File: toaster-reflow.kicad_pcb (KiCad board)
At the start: 2 copper layers, 41.9 x 63.5 mm, 40 parts, among them J1 1935161, J2 1935161, J3 Raspberry_Pi_2_3, J4 1935161, J5 1935161, J6 Conn_01x03, K1 1-1415899-3, Q1 Q_PMOS_GSD, Q2 Q_PMOS_GSD, Q3 Q_PMOS_GSD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

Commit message: update pcb
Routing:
- net Net-(J1-Pad2): track 16.7 -> 0.00 mm
- net Net-(J1-Pad1): track 16.7 -> 0.00 mm
- added copper zone on B.Cu, net Net-(J1-Pad1)
- added copper zone on F.Cu, net Net-(J1-Pad1)
- added copper zone on B.Cu, net Net-(J1-Pad2)
- added copper zone on F.Cu, net Net-(J1-Pad2)
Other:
- outline, holes or cut-outs redrawn
- net class AC_Load: clearance 0.2 -> 1
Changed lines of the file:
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@@
   (general
     (thickness 1.6)
-    (drawings 20)
-    (tracks 363)
+    (drawings 8)
+    (tracks 357)
     (zones 0)
     (modules 40)
@@
     (last_trace_width 0.25)
     (trace_clearance 0.2)
-    (zone_clearance 0.508)
+    (zone_clearance 2)
     (zone_45_only no)
     (trace_min 0.2)
@@
   )
   (net_class AC_Load ""
-    (clearance 0.2)
+    (clearance 1)
     (trace_width 3)
     (via_dia 0.8)
@@
     (add_net "Net-(C7-Pad2)")
     (add_net "Net-(C8-Pad2)")
+  )
+  (module 1935161:PHOENIX_1935161 (layer F.Cu)
+    (at 132.08 93.98 90)
+    (fp_text reference J1 (at 0 0 90) (layer F.SilkS)
+      (effects (font (size 1 0.9) (thickness 0.05)))
+    )
+    (fp_text value 1935161 (at 0 0 90) (layer F.SilkS)
+      (effects (font (size 1 0.9) (thickness 0.05)))
+    )
+    (fp_line (start -5 -4) (end 5 -4) (layer F.SilkS) (width 0.127))
+    (fp_line (start 5 -4) (end 5 4.3) (layer F.SilkS) (width 0.127))
+    (fp_line (start 5 4.3) (end -5 4.3) (layer F.SilkS) (width 0.127))
+    (fp_line (start -5 4.3) (end -5 -4) (layer F.SilkS) (width 0.127))
+    (fp_line (start -5 4.3) (end -5 -4) (layer Dwgs.User) (width 0.127))
+    (fp_line (start -5 -4) (end 5 -4) (layer Dwgs.User) (width 0.127))
+    (fp_line (start 5 -4) (end 5 4.3) (layer Dwgs.User) (width 0.127))
+    (fp_line (start 5 4.3) (end -5 4.3) (layer Dwgs.User) (width 0.127))
+    (fp_circle (center -3.8 -1.5) (end -3.66 -1.5) (layer F.SilkS) (width 0.28))
+    (fp_circle (center -3.8 -1.5) (end -3.66 -1.5) (layer Dwgs.User) (width 0.28))
+    (fp_line (start -5.25 -4.25) (end 5.25 -4.25) (layer Eco1.User) (width 0.05))
+    (fp_line (start 5.25 -4.25) (end 5.25 4.55) (layer Eco1.User) (width 0.05))
+    (fp_line (start 5.25 4.55) (end -5.25 4.55) (layer Eco1.User) (width 0.05))
+    (fp_line (start -5.25 4.55) (end -5.25 -4.25) (layer Eco1.User) (width 0.05))
+    (fp_text user NAME (at -5.090826 -5.090826 90) (layer Cmts.User)
+      (effects (font (size 1 1) (thickness 0.05)))
+    )
+    (fp_text user VALUE (at -5.093458 6.366825 90) (layer Eco2.User)
+      (effects (font (size 1 1) (thickness 0.05)))
+    )
+    (pad 1 thru_hole rect (at -2.5 0 90) (size 1.95 1.95) (drill 1.3) (layers *.Cu *.Mask)
+      (net 16 "Net-(J1-Pad1)"))
+    (pad 2 thru_hole circle (at 2.5 0 90) (size 1.95 1.95) (drill 1.3) (layers *.Cu *.Mask)
+      (net 17 "Net-(J1-Pad2)"))
   )
   (module Capacitor_SMD:C_0603_1608Metric (layer F.Cu)
@@
       (rotate (xyz 0 0 0))
     )
-  )
-  (module 1935161:PHOENIX_1935161 (layer F.Cu)
-    (at 132.08 93.98 90)
-    (fp_text reference J1 (at 0 0 90) (layer F.SilkS)
-      (effects (font (size 1 0.9) (thickness 0.05)))
-    )
-    (fp_text value 1935161 (at 0 0 90) (layer F.SilkS)
-      (effects (font (size 1 0.9) (thickness 0.05)))
-    )
-    (fp_line (start -5 -4) (end 5 -4) (layer F.SilkS) (width 0.127))
-    (fp_line (start 5 -4) (end 5 4.3) (layer F.SilkS) (width 0.127))
-    (fp_line (start 5 4.3) (end -5 4.3) (layer F.SilkS) (width 0.127))
-    (fp_line (start -5 4.3) (end -5 -4) (layer F.SilkS) (width 0.127))
-    (fp_line (start -5 4.3) (end -5 -4) (layer Dwgs.User) (width 0.127))
-    (fp_line (start -5 -4) (end 5 -4) (layer Dwgs.User) (width 0.127))
-    (fp_line (start 5 -4) (end 5 4.3) (layer Dwgs.User) (width 0.127))
-    (fp_line (start 5 4.3) (end -5 4.3) (layer Dwgs.User) (width 0.127))
-    (fp_circle (center -3.8 -1.5) (end -3.66 -1.5) (layer F.SilkS) (width 0.28))
-    (fp_circle (center -3.8 -1.5) (end -3.66 -1.5) (layer Dwgs.User) (width 0.28))
-    (fp_line (start -5.25 -4.25) (end 5.25 -4.25) (layer Eco1.User) (width 0.05))
-    (fp_line (start 5.25 -4.25) (end 5.25 4.55) (layer Eco1.User) (width 0.05))
-    (fp_line (start 5.25 4.55) (end -5.25 4.55) (layer Eco1.User) (width 0.05))
-    (fp_line (start -5.25 4.55) (end -5.25 -4.25) (layer Eco1.User) (width 0.05))
-    (fp_text user NAME (at -5.090826 -5.090826 90) (layer Cmts.User)
-      (effects (font (size 1 1) (thickness 0.05)))
-    )
-    (fp_text user VALUE (at -5.093458 6.366825 90) (layer Eco2.User)
-      (effects (font (size 1 1) (thickness 0.05)))
-    )
-    (pad 1 thru_hole rect (at -2.5 0 90) (size 1.95 1.95) (drill 1.3) (layers *.Cu *.Mask)
-      (net 16 "Net-(J1-Pad1)"))
-    (pad 2 thru_hole circle (at 2.5 0 90) (size 1.95 1.95) (drill 1.3) (layers *.Cu *.Mask)
-      (net 17 "Net-(J1-Pad2)"))
   )
   (module 1935161:PHOENIX_1935161 (layer F.Cu)
@@
     )
   )
-  (gr_arc (start 129.794 93.98) (end 129.794 93.472) (angle -180) (layer Edge.Cuts) (width 0.2))
-  (gr_arc (start 150.876 93.472) (end 150.876 93.98) (angle -180) (layer Edge.Cuts) (width 0.2))
-  (gr_line (start 148.844 92.964) (end 150.876 92.964) (layer Edge.Cuts) (width 0.2))
-  (gr_line (start 148.844 93.98) (end 150.876 93.98) (layer Edge.Cuts) (width 0.2))
-  (gr_line (start 132.08 94.488) (end 129.794 94.488) (layer Edge.Cuts) (width 0.2))
-  (gr_line (start 132.08 93.472) (end 129.794 93.472) (layer Edge.Cuts) (width 0.2))
-  (gr_line (start 132.08 94.488) (end 137.414 94.488) (layer Edge.Cuts) (width 0.2))
-  (gr_line (start 137.414 93.472) (end 132.08 93.472) (layer Edge.Cuts) (width 0.2))
-  (gr_line (start 140.97 92.964) (end 137.414 93.472) (layer Edge.Cuts) (width 0.2))
-  (gr_line (start 148.844 92.964) (end 140.97 92.964) (layer Edge.Cuts) (width 0.2))
-  (gr_line (start 140.97 93.98) (end 148.844 93.98) (layer Edge.Cuts) (width 0.2))
-  (gr_line (start 137.414 94.488) (end 140.97 93.98) (layer Edge.Cuts) (width 0.2))
   (gr_text Heating (at 128.27 123.19) (layer F.SilkS)
     (effects (font (size 1.5 1.5) (thickness 0.3)) (justify left))
@@
   (segment (start 156.9975 137.16) (end 157.48 136.6775) (width 0.25) (layer F.Cu) (net 15))
   (segment (start 153.1875 137.16) (end 156.9975 137.16) (width 0.25) (layer F.Cu) (net 15))
-  (segment (start 148.53 95.99) (end 141.03 95.99) (width 3) (layer B.Cu) (net 16) (status 30))
-  (segment (start 140.54 96.48) (end 132.08 96.48) (width 3) (layer B.Cu) (net 16) (status 30))
-  (segment (start 141.03 95.99) (end 140.54 96.48) (width 3) (layer B.Cu) (net 16) (status 30))
-  (segment (start 132.61 90.95) (end 141.03 90.95) (width 3) (layer B.Cu) (net 17) (status 30))
-  (segment (start 132.08 91.48) (end 132.61 90.95) (width 3) (layer B.Cu) (net 17) (status 30))
-  (segment (start 141.03 90.95) (end 148.53 90.95) (width 3) (layer B.Cu) (net 17) (status 30))
   (segment (start 157.2675 100.6) (end 157.48 100.8125) (width 0.25) (layer F.Cu) (net 24) (status 30))
   (segment (start 154.62 100.6) (end 157.2675 100.6) (width 0.25) (layer F.Cu) (net 24) (status 30))
@@
     )
   )
-  (zone (net 0) (net_name "") (layers F&B.Cu) (hatch edge 0.508)
-    (connect_pads (clearance 0.508))
+  (zone (net 16) (net_name "Net-(J1-Pad1)") (layer F.Cu) (hatch edge 0.508)
+    (priority 1)
+    (connect_pads yes (clearance 2))
     (min_thickness 0.254)
-    (keepout (tracks allowed) (vias allowed) (copperpour not_allowed))
-    (fill (arc_segments 16) (thermal_gap 0.508) (thermal_bridge_width 0.508))
+    (fill yes (arc_segments 16) (thermal_gap 0.25) (thermal_bridge_width 0.508))
     (polygon
       (pts
-        (xy 127.508 88.138) (xy 152.146 88.138) (xy 152.146 99.06) (xy 127.508 99.06)
+        (xy 127 94.742) (xy 127 100.33) (xy 150.114 100.33) (xy 150.114 94.234) (xy 140.97 94.234)
+        (xy 137.668 94.742)
       )
     )
+  )
+  (zone (net 17) (net_name "Net-(J1-Pad2)") (layer F.Cu) (hatch edge 0.508)
+    (priority 1)
+    (connect_pads yes (clearance 2))
+    (min_thickness 0.254)
+    (fill yes (arc_segments 16) (thermal_gap 1) (thermal_bridge_width 0.508))
+    (polygon
+      (pts
+        (xy 150.114 92.71) (xy 140.97 92.71) (xy 137.414 93.218) (xy 127 93.218) (xy 127 87.63)
+        (xy 150.114 87.63)
+      )
+    )
+  )
+  (zone (net 17) (net_name "Net-(J1-Pad2)") (layer B.Cu) (hatch edge 0.508)
+    (priority 2)
+    (connect_pads yes (clearance 2))
+    (min_thickness 0.254)
+    (fill yes (arc_segments 16) (thermal_gap 1) (thermal_bridge_width 0.508))
+    (polygon
+      (pts
+        (xy 127 87.63) (xy 150.114 87.63) (xy 150.114 92.71) (xy 140.97 92.71) (xy 137.668 93.218)
+        (xy 127 93.218)
+      )
+    )
+  )
+  (zone (net 16) (net_name "Net-(J1-Pad1)") (layer B.Cu) (hatch edge 0.508)
+    (priority 2)
+    (connect_pads yes (clearance 2))
+    (min_thickness 0.254)
+    (fill yes (arc_segments 16) (thermal_gap 1) (thermal_bridge_width 0.508))
+    (polygon
+      (pts
+        (xy 127 94.742) (xy 137.922 94.742) (xy 140.97 94.234) (xy 150.114 94.234) (xy 150.114 100.33)
+        (xy 127 100.33)
+      )
+    )

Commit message: Add a bunch of stuff
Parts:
- removed J5: 1935161, 1935161:PHOENIX_1935161
- removed Q5: Q_PMOS_GSD, Package_TO_SOT_SMD:SOT-23
- added R10: 100, Resistor_SMD:R_0603_1608Metric, B.Cu at (125.2, 122.4)
- added R11: 47k, Resistor_SMD:R_0603_1608Metric, B.Cu at (147.8, 123.7)
- added R9: 100, Resistor_SMD:R_0603_1608Metric, B.Cu at (133.3, 118.4)
- C1, C2, C3, C4, C7, C8, C9, D1, R1, R4, R5, U1, U2, U3: moved to B.Cu
- J4: value 1935161 -> Conn_01x04; footprint 1935161:PHOENIX_1935161 -> 1990025:1990025
- Q1, Q2: value Q_PMOS_GSD -> Q_NMOS_GSD; footprint Package_TO_SOT_SMD:SOT-23 -> Package_TO_SOT_SMD:SC-59; moved to B.Cu
- Q3, Q4: value Q_PMOS_GSD -> Q_PNP_BEC; footprint Package_TO_SOT_SMD:SOT-23 -> Package_TO_SOT_SMD:SC-59; moved to B.Cu
- R2: value 470 -> 1K
- R6: value 10K -> 100; moved to B.Cu
- R7: value 470 -> 100; moved to B.Cu
- R8: value 470 -> 47k; moved to B.Cu
- moved R7 44.8 mm to (126.5, 112.0), turned to 270 degrees
- moved D4 36.4 mm to (137.7, 116.8)
- moved C2 36.0 mm to (133.1, 113.0), turned to 180 degrees
- moved C6 35.2 mm to (142.0, 112.8), turned to 180 degrees
- moved J2 34.3 mm to (128.8, 99.8), turned to 270 degrees
- moved C3 34.2 mm to (128.5, 112.0)
- moved C5 33.8 mm to (140.2, 114.8), turned to 180 degrees
- moved D2 32.1 mm to (126.2, 88.9)
- moved R2 31.9 mm to (131.3, 88.9)
- moved R6 31.1 mm to (129.3, 114.8), turned to 0 degrees
- moved C4 30.4 mm to (133.1, 111.0), turned to 0 degrees
- moved U2 29.4 mm to (140.5, 115.6)
- moved J6 28.3 mm to (131.3, 106.9), turned to 270 degrees
- moved J3 26.3 mm to (157.0, 74.9)
- moved C7 24.2 mm to (124.5, 117.3), turned to 0 degrees
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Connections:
- D1 pad 1: Net-(D1-Pad1) -> +5V
- D1 pad 2: GND -> Net-(D1-Pad2)
- D2 pad 2: Net-(D1-Pad1) -> +5V
- D3 pad 1: Net-(D3-Pad1) -> GND
- D3 pad 2: +3V3 -> Net-(D3-Pad2)
- D4 pad 1: Net-(D4-Pad1) -> GND
- D5 pad 1: Net-(D5-Pad1) -> GND
- J2 pad 1: GND -> +5V
- J2 pad 2: +5V -> GND
- J4 pad 1: Net-(C3-Pad2) -> /Thermocouple2/T-
- J4 pad 2: Net-(C2-Pad2) -> /Thermocouple2/T+
- J6 pad 1: Net-(J6-Pad1) -> /SERVO_PWM
- K1 pad 11_1: Net-(J1-Pad1) -> Net-(J1-Pad2)
- K1 pad 11_2: Net-(J1-Pad1) -> Net-(J1-Pad2)
- K1 pad 14_1: Net-(J1-Pad2) -> Net-(J1-Pad1)
- K1 pad 14_2: Net-(J1-Pad2) -> Net-(J1-Pad1)
- K1 pad A1: Net-(D1-Pad1) -> +5V
- K1 pad A2: GND -> Net-(D1-Pad2)
- LS1 pad 2: GND -> Net-(LS1-Pad2)
- Q1 pad 2: Net-(D1-Pad1) -> GND
- Q1 pad 3: +3V3 -> Net-(D1-Pad2)
- Q2 pad 2: Net-(LS1-Pad1) -> GND
- Q2 pad 3: +3V3 -> Net-(LS1-Pad2)
- Q3 pad 1: /SERVO_PWM -> Net-(Q3-Pad1)
- Q3 pad 2: Net-(J6-Pad1) -> Net-(D4-Pad2)
- Q4 pad 1: /THERMO1_FAULT -> Net-(Q4-Pad1)
- Q4 pad 2: Net-(D4-Pad2) -> Net-(D5-Pad2)
- R1 pad 1: +3V3 -> /HEAT_ENABLE
- R1 pad 2: /HEAT_ENABLE -> GND
- R2 pad 1: GND -> Net-(D1-Pad2)
- R3 pad 1: GND -> Net-(D3-Pad2)
- R3 pad 2: Net-(D3-Pad1) -> +3V3
- R4 pad 1: +3V3 -> /BUZZER
- R4 pad 2: /BUZZER -> GND
- R5 pad 2: GND -> Net-(LS1-Pad2)
- R6 pad 1: +3V3 -> Net-(C2-Pad2)
- R6 pad 2: /SERVO_PWM -> /Thermocouple1/T+
- R7 pad 1: GND -> Net-(C3-Pad2)
- R7 pad 2: Net-(D4-Pad1) -> /Thermocouple1/T-
- R8 pad 1: GND -> Net-(Q3-Pad1)
- R8 pad 2: Net-(D5-Pad1) -> /THERMO1_FAULT
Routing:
- net GND: track 14.5 -> 202.0 mm, vias 6 -> 10
- net +5V: track 73.1 -> 119.5 mm, vias 1 -> 2
- net /BUZZER: track 43.5 -> 10.3 mm, vias 2 -> 0
- net Net-(D1-Pad1): track 30.7 -> 0.00 mm, vias 2 -> 0
- net Net-(D1-Pad2): track 0.00 -> 24.7 mm, vias 0 -> 3
- net /SERVO_PWM: track 21.2 -> 44.7 mm, vias 2 -> 0
- net /THERMO2_DRDY: track 43.3 -> 60.5 mm, vias 3 -> 1
- net /THERMO1_CS: track 45.3 -> 31.4 mm, vias 0 -> 2
- net Net-(J6-Pad1): track 13.8 -> 0.00 mm, vias 1 -> 0
- net Net-(LS1-Pad1): track 16.5 -> 2.85 mm, vias 1 -> 0
- net /THERMO1_DRDY: track 48.0 -> 35.6 mm
- net Net-(Q3-Pad1): track 0.00 -> 12.3 mm, vias 0 -> 2
- net /THERMO2_FAULT: track 30.8 -> 42.6 mm, vias 3 -> 0
- net Net-(D5-Pad2): track 5.23 -> 16.6 mm, vias 0 -> 1
- net Net-(C3-Pad2): track 22.5 -> 33.5 mm, vias 1 -> 0
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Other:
- board size 41.9 x 63.5 mm -> 40.1 x 51.8 mm
- board text added: "+"
- board text added: "-"
- board text added: "5V"
- board text added: "LOAD"
- board text added: "PWR"
- board text added: "S"
- board text removed: "- 5V +"
- board text removed: "Heating"
- board text removed: "Power"
- board text removed: "Servo"

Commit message: update pcb for 3d rendering
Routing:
- net GND: track 202.0 -> 180.9 mm
- net +3V3: track 111.7 -> 112.9 mm
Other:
- board text added: "1"
- board text added: "2"
- board text added: "Thermocouples"
- board text removed: "S"

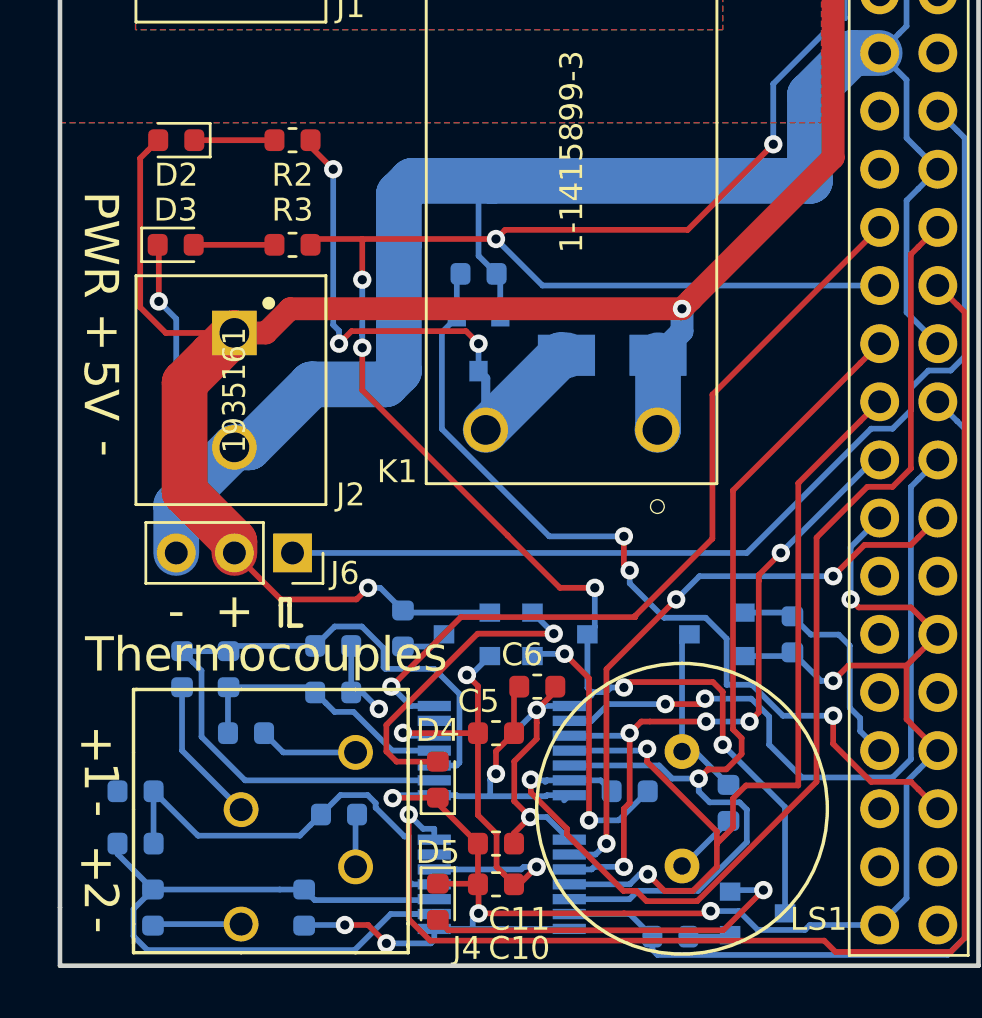
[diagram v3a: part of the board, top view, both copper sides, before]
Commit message: UPdate transistor wiring
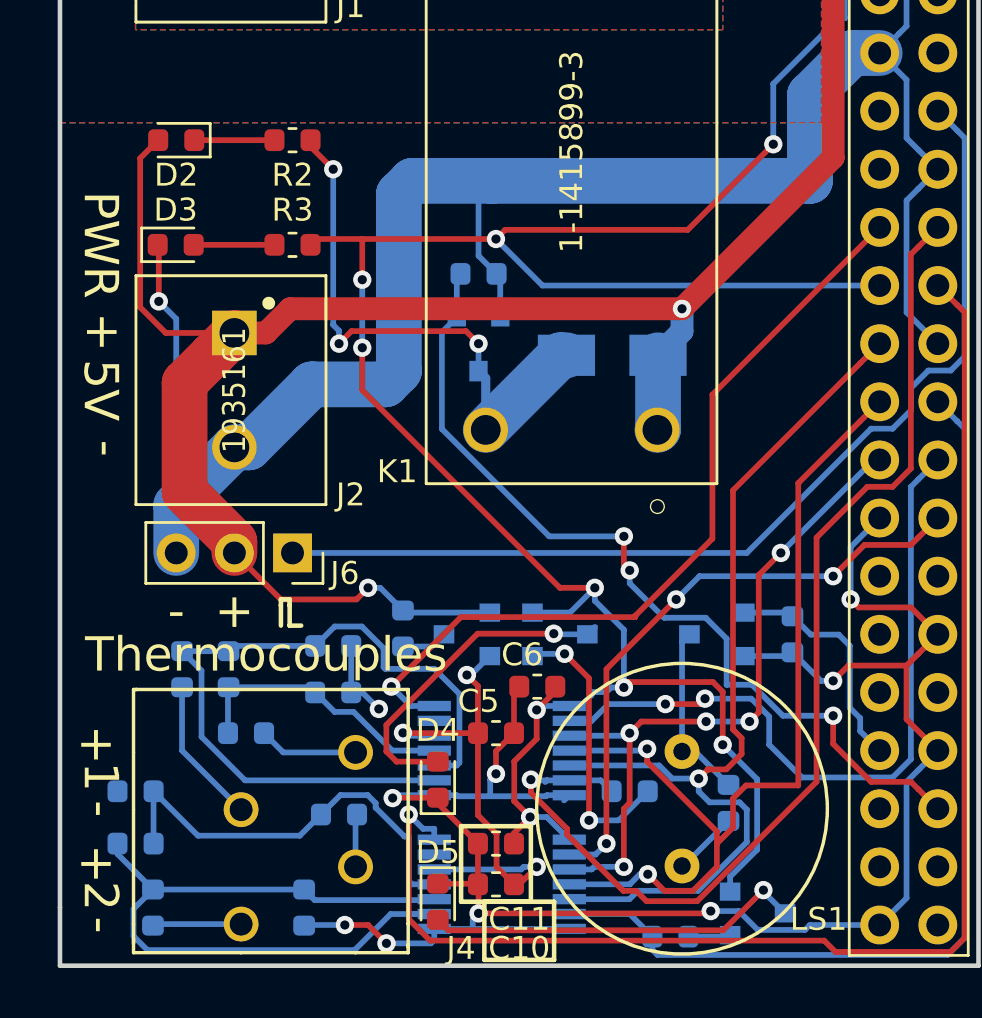
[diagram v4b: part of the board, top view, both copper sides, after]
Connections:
- Q3 pad 2: Net-(D4-Pad2) -> +3V3
- Q3 pad 3: +3V3 -> Net-(D4-Pad2)
- Q4 pad 2: Net-(D5-Pad2) -> +3V3
- Q4 pad 3: +3V3 -> Net-(D5-Pad2)
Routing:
- net +3V3: track 112.9 -> 114.3 mm
- net Net-(D4-Pad2): track 13.9 -> 14.5 mm
